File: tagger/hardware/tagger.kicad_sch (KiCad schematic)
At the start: 34 parts, among them J10 TETHER_TX, J11 TETHER_RX, J4 SWD, J8 DISPLAY, J9 IO_CONN, Q1 Q_NMOS_GSD, SW24 BOOT0, SW26 NRST, U2 STM32F103RGTx, U3 LTC2851xDD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

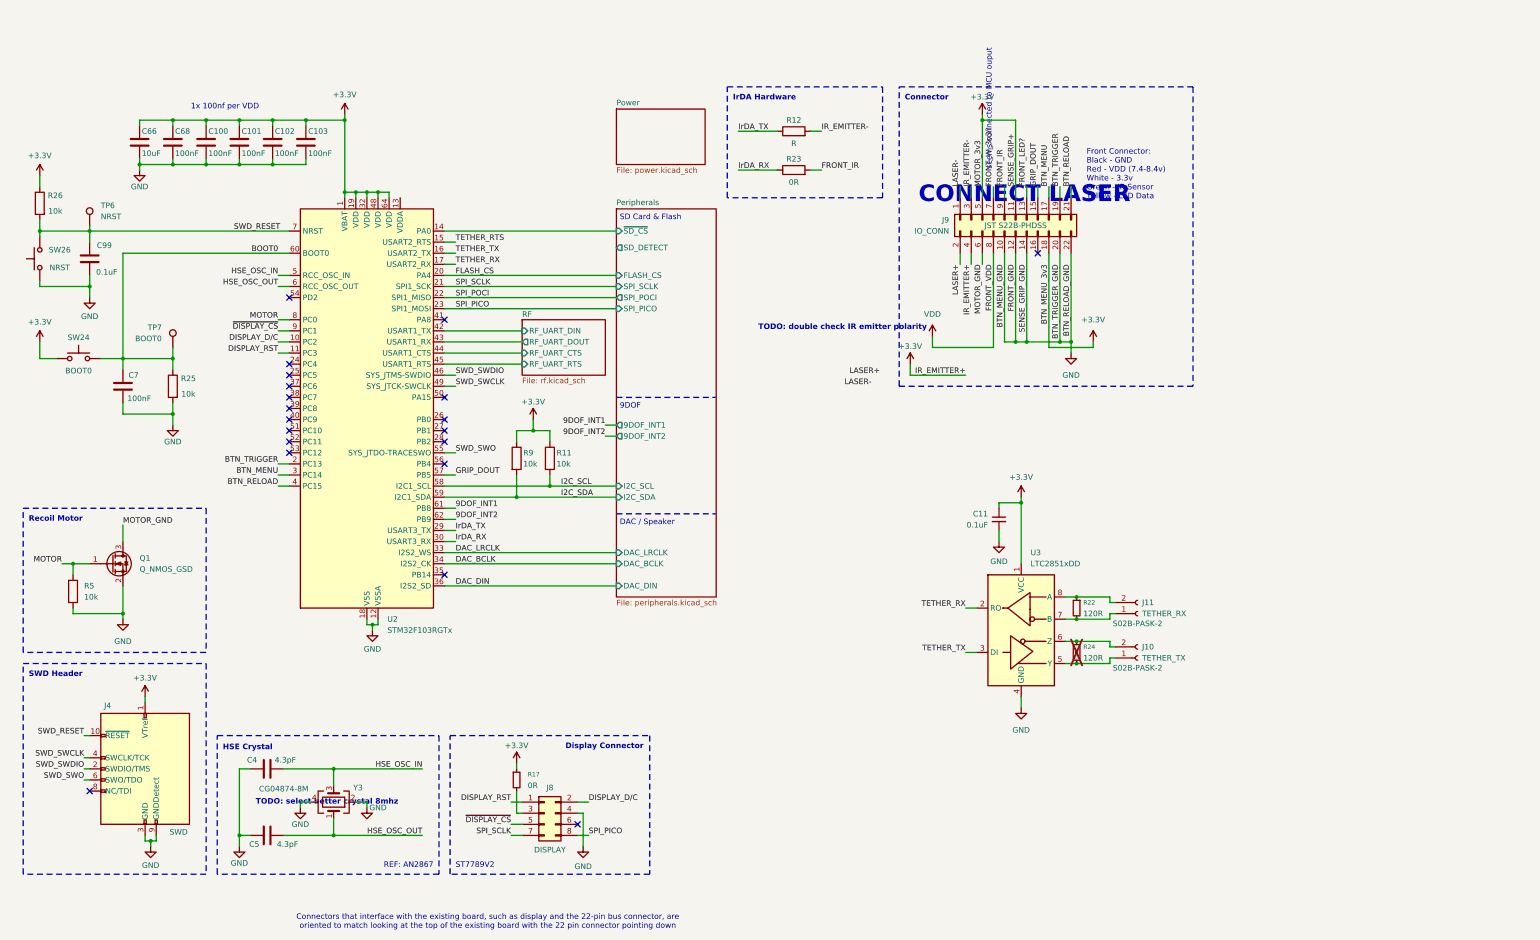
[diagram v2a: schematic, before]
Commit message: feat: schematic organization, added SD card connections
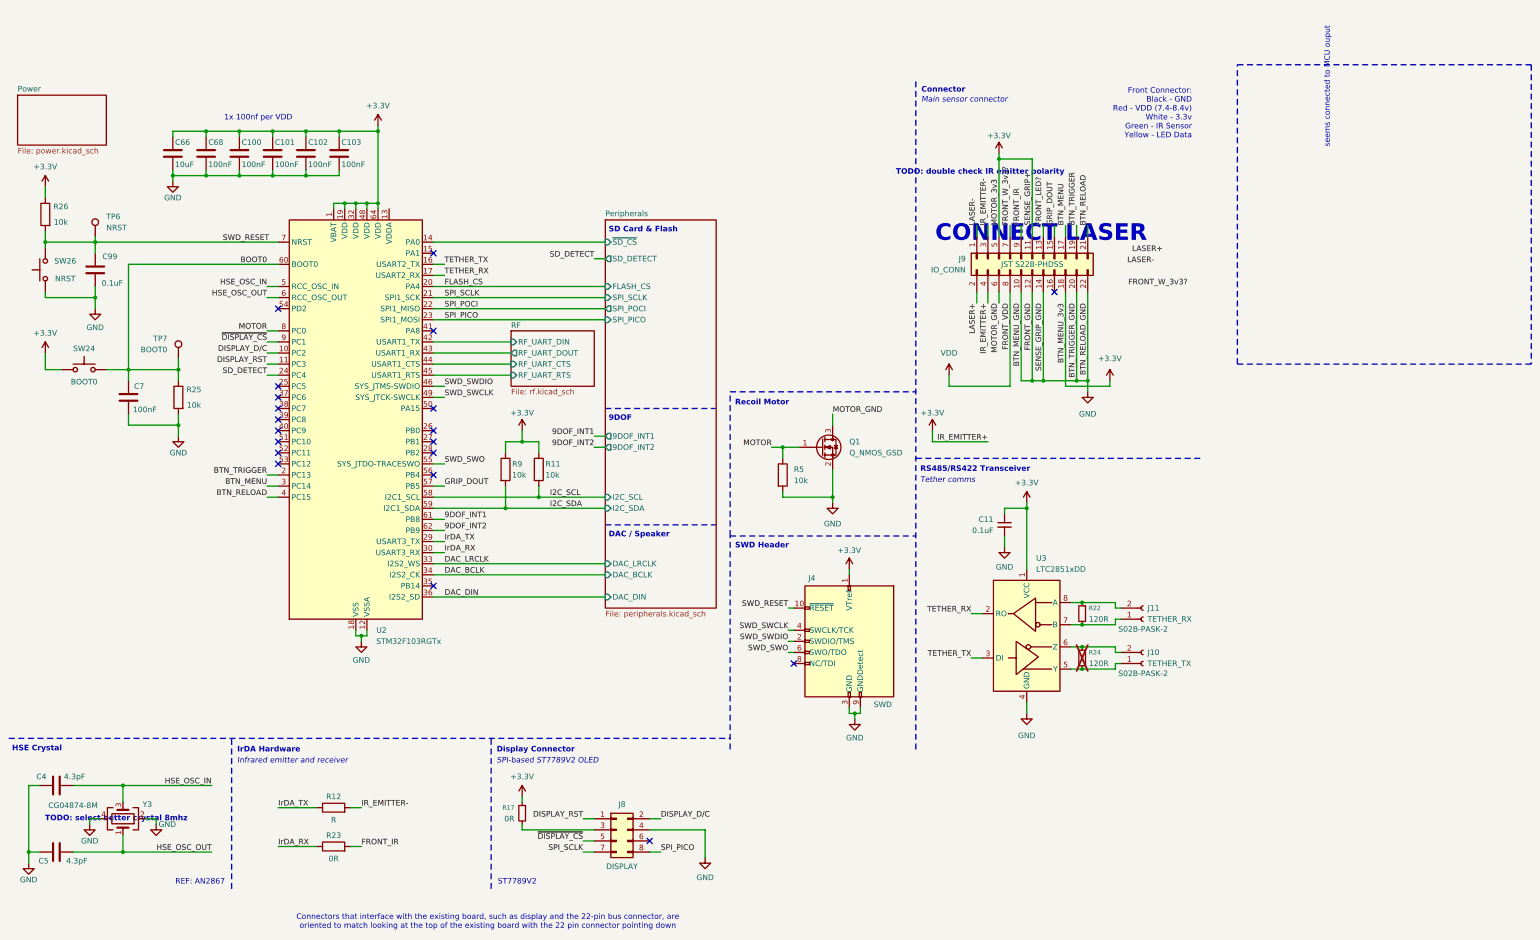
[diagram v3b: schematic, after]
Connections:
- net SD_DETECT: now reaches U2.24 (PC4)
- net TETHER_RTS: no longer names the net of U2.15 (PA1)
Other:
- note added: "Infrared emitter and receiver"
- note added: "Main sensor connector"
- note added: "RS485/RS422 Transceiver"
- note added: "SPI-based ST7789V2 OLED"
- note added: "Tether comms"
- moved on the sheet: C100, C101, C102, C103, C11, C4, C5, C66, C68, C7, C99, J10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

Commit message: feat: replace RS485 transceiver, fix DRC warnings
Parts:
- removed TP6: NRST, TestPoint:TestPoint_Pad_D1.5mm, symbol Connector:TestPoint
- removed TP7: BOOT0, TestPoint:TestPoint_Pad_D1.5mm, symbol Connector:TestPoint
- removed U3: LTC2851xDD, Package_DFN_QFN:DFN-8-1EP_3x3mm_P0.5mm_EP1.66x2.38mm, symbol Interface_UART:LTC2851xDD
- added U3: LTC2852xDD, Package_DFN_QFN:DFN-10-1EP_3x3mm_P0.5mm_EP1.65x2.38mm, symbol Interface_UART:LTC2852xDD
- J10, J11, J4, J8, J9: now not fitted
- R22, R24: footprint (none) -> Resistor_SMD:R_0603_1608Metric_Pad0.98x0.95mm_HandSolder
- SW24: value BOOT0 -> B0
- SW26: value NRST -> RST
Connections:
- net +3.3V: now also U3.10 (VCC)
- net GND: now also U3.11 (GND), U3.5 (GND)
- net TETHER_RX: now also U3.1 (RO)
- net TETHER_TX: now also U3.4 (DI)
- net at J10.1 (Pin_1), R24.2: now also U3.6 (Y)
- net at J10.2 (Pin_2), R24.1: now also U3.7 (Z)
- net at J11.1 (Pin_1), R22.2: now also U3.8 (B)
- net at J11.2 (Pin_2), R22.1: now also U3.9 (A)
- net TETHER_DRIV_EN: now reaches U2.37 (PC6)
- net TETHER_DRIV_EN: now also U3.3 (DE)
- net TETHER_RECV_EN: now reaches U2.38 (PC7)
- net TETHER_RECV_EN: now also U3.2 (~{RE})
- no-connect marks 20 -> 18
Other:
- note added: "2: WHITE 1: BLUE"
- note added: "2: YELLOW 1: GREEN"
- moved on the sheet: C11, R22, R24, R25
